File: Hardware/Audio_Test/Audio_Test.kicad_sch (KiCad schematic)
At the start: 1 part, among them U1 HPM6P41IPB1

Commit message: 第二次提交，完成了系统的基本构建
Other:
- removed sheet hpm6p41_Core
- moved on the sheet: U1A, U1B, U1C, U1D, U1E, U1F
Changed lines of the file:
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@@
 	(symbol
 		(lib_id "HPM6P00_Library:HPM6P41IPB1")
-		(at -605.79 100.33 0)
+		(at -250.19 34.29 0)
 		(unit 4)
 		(exclude_from_sim no)
@@
 		(fields_autoplaced yes)
 		(property "Reference" "U1"
-			(at -419.1 145.4149 0)
+			(at -63.5 79.3749 0)
 			(effects
 				(font
@@
 		)
 		(property "Value" "HPM6P41IPB1"
-			(at -419.1 147.9549 0)
+			(at -63.5 81.9149 0)
 			(effects
 				(font
@@
 		)
 		(property "Footprint" "HPM_footprints:LQFP-100_14x14mm_P0.5mm_EP5.0x5.0mm"
-			(at -574.04 93.98 0)
+			(at -218.44 27.94 0)
 			(effects
 				(font
@@
 		)
 		(property "Datasheet" ""
-			(at -605.79 100.33 0)
+			(at -250.19 34.29 0)
 			(effects
 				(font
@@
 		)
 		(property "Description" "eLQFP100"
-			(at -605.79 100.33 0)
+			(at -250.19 34.29 0)
 			(effects
 				(font
@@
 	(symbol
 		(lib_id "HPM6P00_Library:HPM6P41IPB1")
-		(at -712.47 146.05 0)
+		(at -356.87 80.01 0)
 		(unit 1)
 		(exclude_from_sim no)
@@
 		(fields_autoplaced yes)
 		(property "Reference" "U1"
-			(at -694.69 140.97 0)
+			(at -339.09 74.93 0)
 			(effects
 				(font
@@
 		)
 		(property "Value" "HPM6P41IPB1"
-			(at -694.69 143.51 0)
+			(at -339.09 77.47 0)
 			(effects
 				(font
@@
 		)
 		(property "Footprint" "HPM_footprints:LQFP-100_14x14mm_P0.5mm_EP5.0x5.0mm"
-			(at -680.72 139.7 0)
+			(at -325.12 73.66 0)
 			(effects
 				(font
@@
 		)
 		(property "Datasheet" ""
-			(at -712.47 146.05 0)
+			(at -356.87 80.01 0)
 			(effects
 				(font
@@
 		)
 		(property "Description" "eLQFP100"
-			(at -712.47 146.05 0)
+			(at -356.87 80.01 0)
 			(effects
 				(font
@@
 	(symbol
 		(lib_id "HPM6P00_Library:HPM6P41IPB1")
-		(at -605.79 19.05 0)
+		(at -250.19 -46.99 0)
 		(unit 5)
 		(exclude_from_sim no)
@@
 		(fields_autoplaced yes)
 		(property "Reference" "U1"
-			(at -407.67 56.5149 0)
+			(at -52.07 -9.5251 0)
 			(effects
 				(font
@@
 		)
 		(property "Value" "HPM6P41IPB1"
-			(at -407.67 59.0549 0)
+			(at -52.07 -6.9851 0)
 			(effects
 				(font
@@
 		)
 		(property "Footprint" "HPM_footprints:LQFP-100_14x14mm_P0.5mm_EP5.0x5.0mm"
-			(at -574.04 12.7 0)
+			(at -218.44 -53.34 0)
 			(effects
 				(font
@@
 		)
 		(property "Datasheet" ""
-			(at -605.79 19.05 0)
+			(at -250.19 -46.99 0)
 			(effects
 				(font
@@
 		)
 		(property "Description" "eLQFP100"
-			(at -605.79 19.05 0)
+			(at -250.19 -46.99 0)
 			(effects
 				(font
@@
 	(symbol
 		(lib_id "HPM6P00_Library:HPM6P41IPB1")
-		(at -711.2 101.6 0)
+		(at -355.6 35.56 0)
 		(unit 6)
 		(exclude_from_sim no)
@@
 		(fields_autoplaced yes)
 		(property "Reference" "U1"
-			(at -693.42 96.52 0)
+			(at -337.82 30.48 0)
 			(effects
 				(font
@@
 		)
 		(property "Value" "HPM6P41IPB1"
-			(at -693.42 99.06 0)
+			(at -337.82 33.02 0)
 			(effects
 				(font
@@
 		)
 		(property "Footprint" "HPM_footprints:LQFP-100_14x14mm_P0.5mm_EP5.0x5.0mm"
-			(at -679.45 95.25 0)
+			(at -323.85 29.21 0)
 			(effects
 				(font
@@
 		)
 		(property "Datasheet" ""
-			(at -711.2 101.6 0)
+			(at -355.6 35.56 0)
 			(effects
 				(font
@@
 		)
 		(property "Description" "eLQFP100"
-			(at -711.2 101.6 0)
+			(at -355.6 35.56 0)
 			(effects
 				(font
@@
 	(symbol
 		(lib_id "HPM6P00_Library:HPM6P41IPB1")
-		(at -605.79 195.58 0)
+		(at -250.19 129.54 0)
 		(unit 3)
 		(exclude_from_sim no)
@@
 		(fields_autoplaced yes)
 		(property "Reference" "U1"
-			(at -457.2 227.9649 0)
+			(at -101.6 161.9249 0)
 			(effects
 				(font
@@
 		)
 		(property "Value" "HPM6P41IPB1"
-			(at -457.2 230.5049 0)
+			(at -101.6 164.4649 0)
 			(effects
 				(font
@@
 		)
 		(property "Footprint" "HPM_footprints:LQFP-100_14x14mm_P0.5mm_EP5.0x5.0mm"
-			(at -574.04 189.23 0)
+			(at -218.44 123.19 0)
 			(effects
 				(font
@@
 		)
 		(property "Datasheet" ""
-			(at -605.79 195.58 0)
+			(at -250.19 129.54 0)
 			(effects
 				(font
@@
 		)
 		(property "Description" "eLQFP100"
-			(at -605.79 195.58 0)
+			(at -250.19 129.54 0)
 			(effects
 				(font
@@
 	(symbol
 		(lib_id "HPM6P00_Library:HPM6P41IPB1")
-		(at -605.79 270.51 0)
+		(at -250.19 204.47 0)
 		(unit 2)
 		(exclude_from_sim no)
@@
 		(fields_autoplaced yes)
 		(property "Reference" "U1"
-			(at -555.625 265.43 0)
+			(at -200.025 199.39 0)
 			(effects
 				(font
@@
 		)
 		(property "Value" "HPM6P41IPB1"
-			(at -555.625 267.97 0)
+			(at -200.025 201.93 0)
 			(effects
 				(font
@@
 		)
 		(property "Footprint" "HPM_footprints:LQFP-100_14x14mm_P0.5mm_EP5.0x5.0mm"
-			(at -574.04 264.16 0)
+			(at -218.44 198.12 0)
 			(effects
 				(font
@@
 		)
 		(property "Datasheet" ""
-			(at -605.79 270.51 0)
+			(at -250.19 204.47 0)
 			(effects
 				(font
@@
 		)
 		(property "Description" "eLQFP100"
-			(at -605.79 270.51 0)
+			(at -250.19 204.47 0)
 			(effects
 				(font
@@
 				)
 			)
-		)
-	)
-	(sheet
-		(at -803.91 -52.07)
-		(size 614.68 393.7)
-		(exclude_from_sim no)
-		(in_bom yes)
-		(on_board yes)
-		(dnp no)
-		(fields_autoplaced yes)
-		(stroke
-			(width 0.1524)
-			(type solid)
-		)
-		(fill
-			(color 0 0 0 0.0000)
-		)
-		(property "Sheetname" "hpm6p41_Core"
-			(at -803.91 -52.7816 0)
-			(effects
-				(font
-					(size 1.27 1.27)
-				)
-				(justify left bottom)
-			)
-		)
-		(property "Sheetfile" "untitled.kicad_sch"
-			(at -803.91 342.2146 0)
-			(effects
-				(font
-					(size 1.27 1.27)
-				)
-				(justify left top)
-			)
-		)
-		(instances
-			(project "Audio_Test"
-				(path "/c78f527e-50e7-4d88-85be-617fff285b50"
-					(page "2")
-				)
-			)

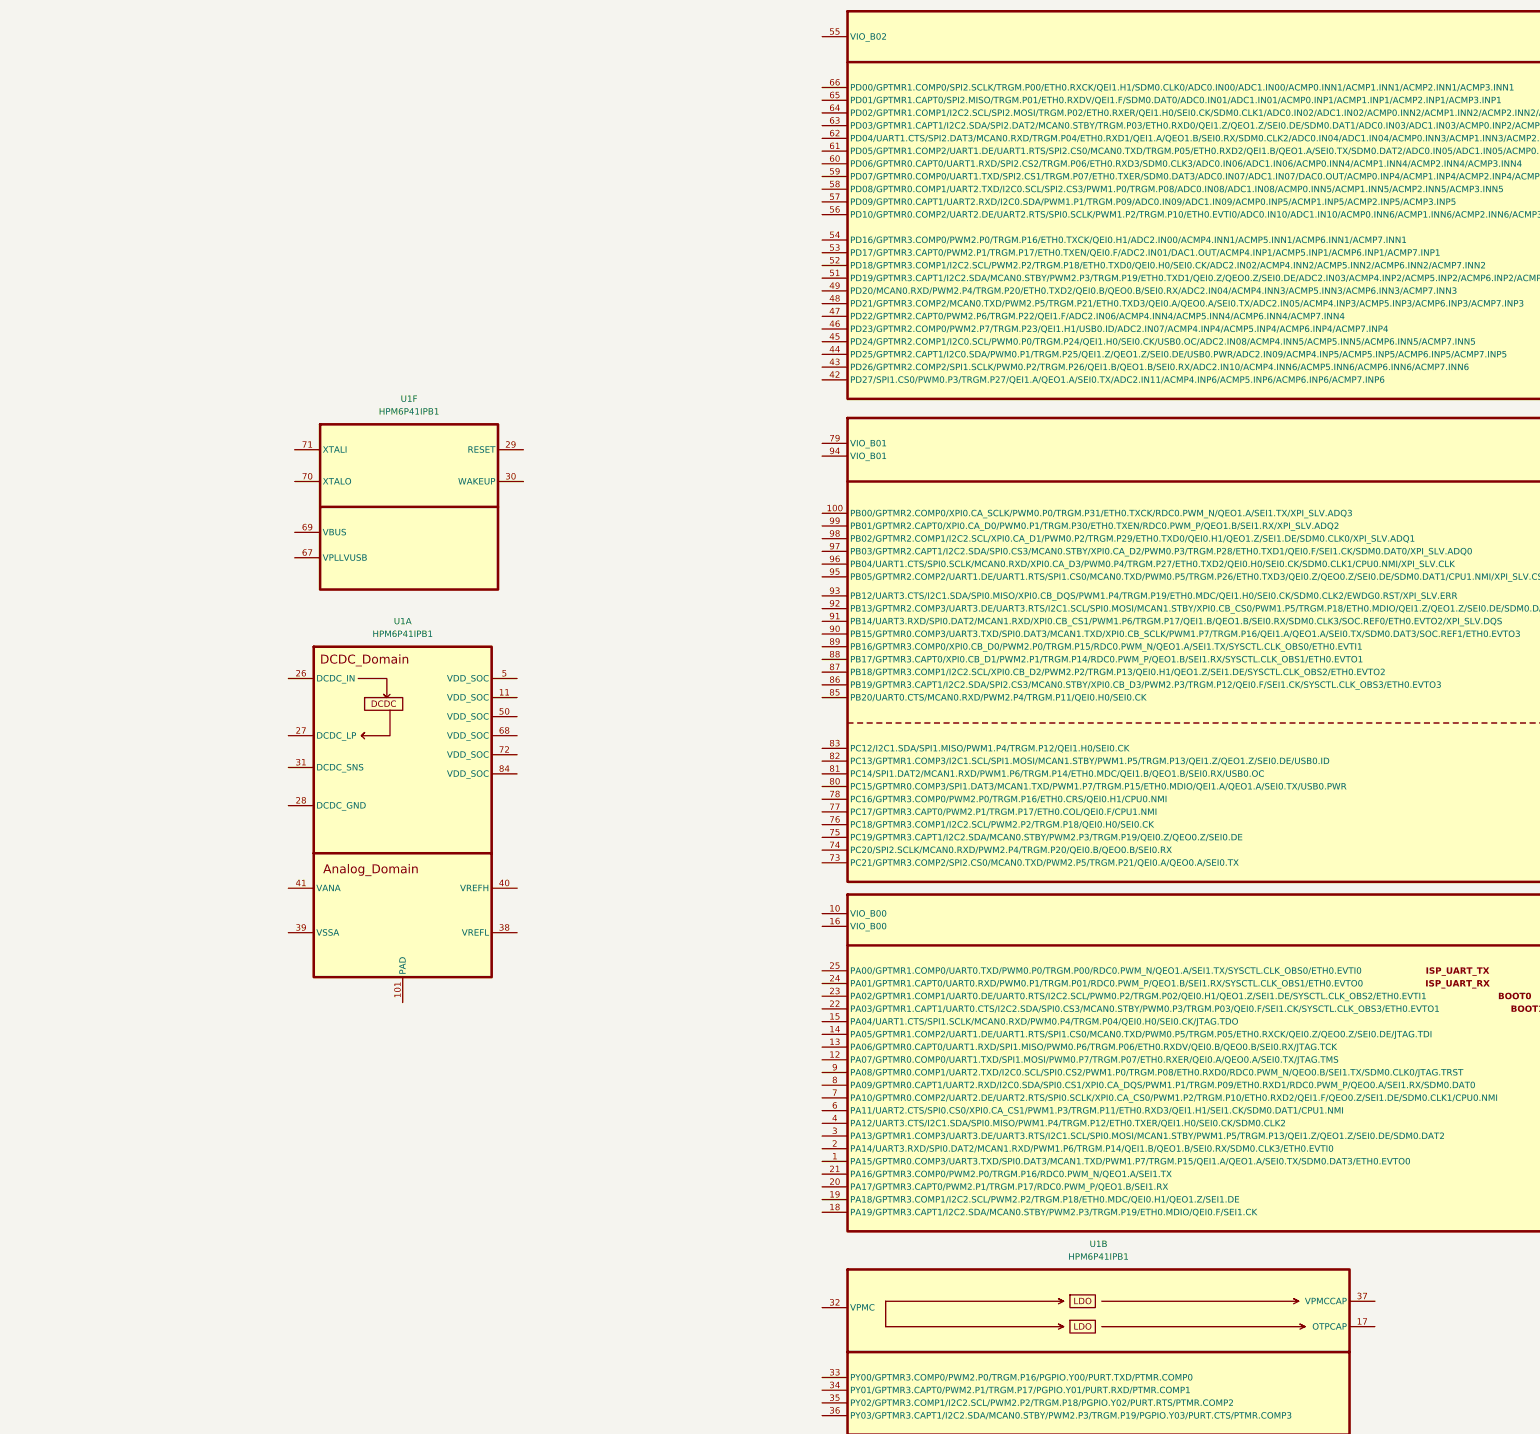
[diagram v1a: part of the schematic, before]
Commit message: 电源网络初步
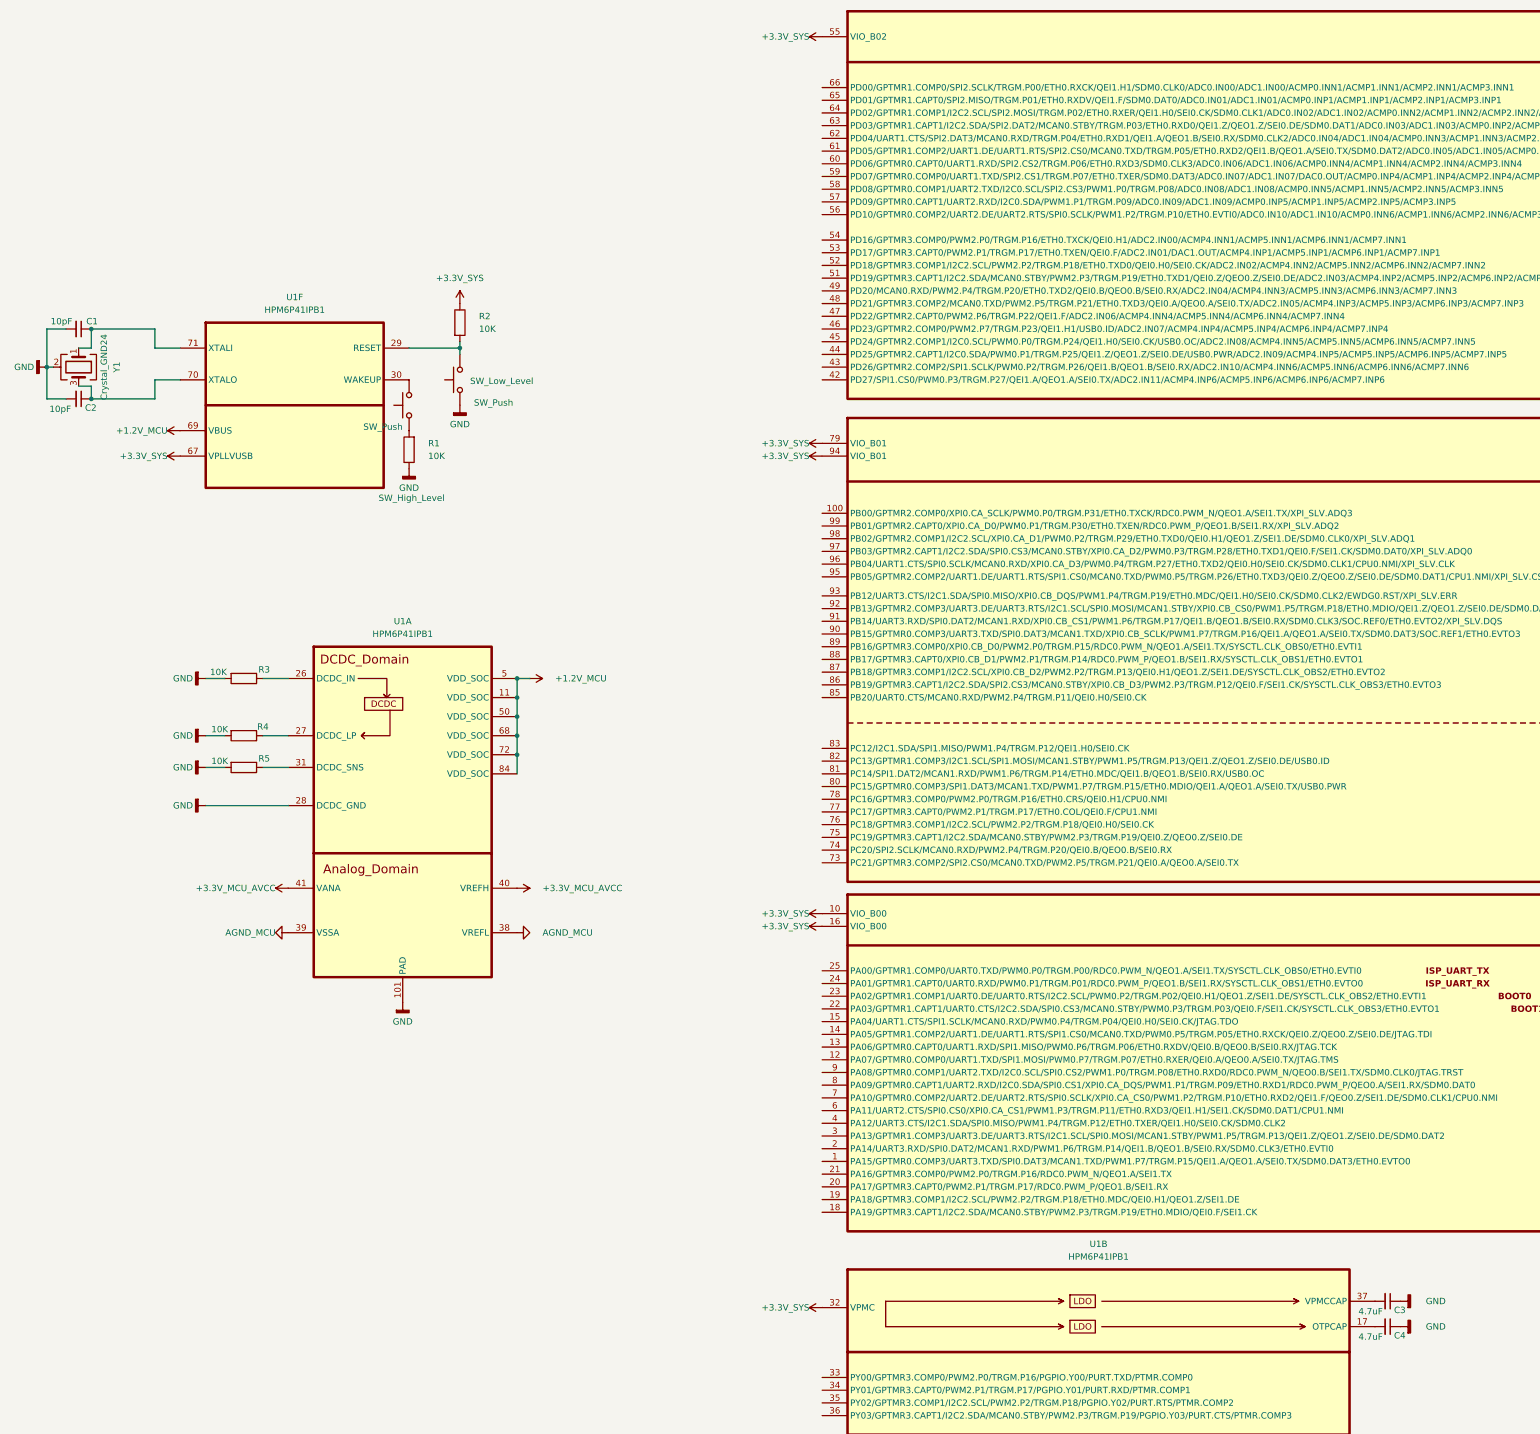
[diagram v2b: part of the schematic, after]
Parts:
- added C1, C2: 10pF, Capacitor_SMD:C_0402_1005Metric, symbol Device:C_Small
- added C3, C4: 4.7uF, Capacitor_SMD:C_0402_1005Metric, symbol Device:C_Small
- added R1, R2, R3, R4, R5: 10K, Resistor_SMD:R_0402_1005Metric, symbol Device:R
- added SW_High_Level, SW_Low_Level: SW_Push, symbol Switch:SW_Push
- added Y1: Crystal_GND24, Crystal:Crystal_SMD_3225-4Pin_3.2x2.5mm, symbol Device:Crystal_GND24
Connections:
- net +3.3V_SYS: now reaches U1.79 (VIO_B01)
- net +3.3V_SYS: now also U1.10 (VIO_B00), U1.16 (VIO_B00), U1.32 (VPMC), U1.55 (VIO_B02), U1.67 (VPLLVUSB), U1.94 (VIO_B01), R2.1
- net GND: now reaches U1.101 (PAD)
- net GND: now also U1.28 (DCDC_GND), C1.2, C2.2, C3.1, C4.1, R1.1, R3.2, R4.2, R5.2, SW_Low_Level.1, Y1.2 (G), Y1.4 (G)
- net +1.2V_MCU: now reaches U1.11 (VDD_SOC)
- net +1.2V_MCU: now also U1.5 (VDD_SOC), U1.50 (VDD_SOC), U1.68 (VDD_SOC), U1.69 (VBUS), U1.72 (VDD_SOC), U1.84 (VDD_SOC)
- net at U1.26 (DCDC_IN): now also R3.1
- net at U1.27 (DCDC_LP): now also R4.1
- net at U1.31 (DCDC_SNS): now also R5.1
- net AGND_MCU: now reaches U1.38 (VREFL)
- net AGND_MCU: now also U1.39 (VSSA)
- net +3.3V_MCU_AVCC: now reaches U1.40 (VREFH)
- net +3.3V_MCU_AVCC: now also U1.41 (VANA)
- net at U1.29 (RESET): now also R2.2, SW_Low_Level.2
- net at U1.30 (WAKEUP): now also SW_High_Level.2
- net at U1.70 (XTALO): now also C2.1, Y1.3
- net at U1.71 (XTALI): now also C1.1, Y1.1
- net at U1.17 (OTPCAP): now also C4.2
- net at U1.37 (VPMCCAP): now also C3.2
- new net: R1.2, SW_High_Level.1
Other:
- moved on the sheet: U1F

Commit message: 电源符号和封装，更换芯片为ES9039Q2M
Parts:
- added U2: ~, Package_DFN_QFN:QFN-32-1EP_5x5mm_P0.5mm_EP3.3x3.3mm, symbol Audio:ES9039Q2M
- added U3, U4: TPS74801DRC, Package_SON:VSON-10-1EP_3x3mm_P0.5mm_EP1.65x2.4mm_ThermalVias, symbol Regulator_Linear:TPS74801DRC
- added U5: ~, ProPrj_Converter_2026-03-10:QFN-10_L3.0-W3.0-P0.45-TL_SILERGY, symbol ProPrj_Converter_2026-03-10:SY8368QNC
- SW1: renamed from SW_Low_Level; footprint (none) -> Button_Switch_SMD:SW_Push_1P1T_NO_Vertical_Wuerth_434133025816
- SW2: renamed from SW_High_Level; footprint (none) -> Button_Switch_SMD:SW_Push_1P1T_NO_Vertical_Wuerth_434133025816
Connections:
- new net: U3.1 (IN), U3.2 (IN)
- new net: U3.10 (OUT), U3.9 (OUT)
- new net: U3.11 (GND), U3.6 (GND)
- new net: U4.1 (IN), U4.2 (IN)
- new net: U4.10 (OUT), U4.9 (OUT)
- new net: U4.11 (GND), U4.6 (GND)
